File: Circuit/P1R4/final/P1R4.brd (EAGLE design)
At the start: 59.7 x 59.7 mm, 88 parts, among them J1 MICRO_USB_B_HIROSE_ZX62R-B-5P, U1 MK20DX256VLH7, U2 TPS61200, U3 MPU-9250, Y1 32.768KHz, Y2 16Mhz/8pF, Y3 26 Mhz, Y4 16 Mhz

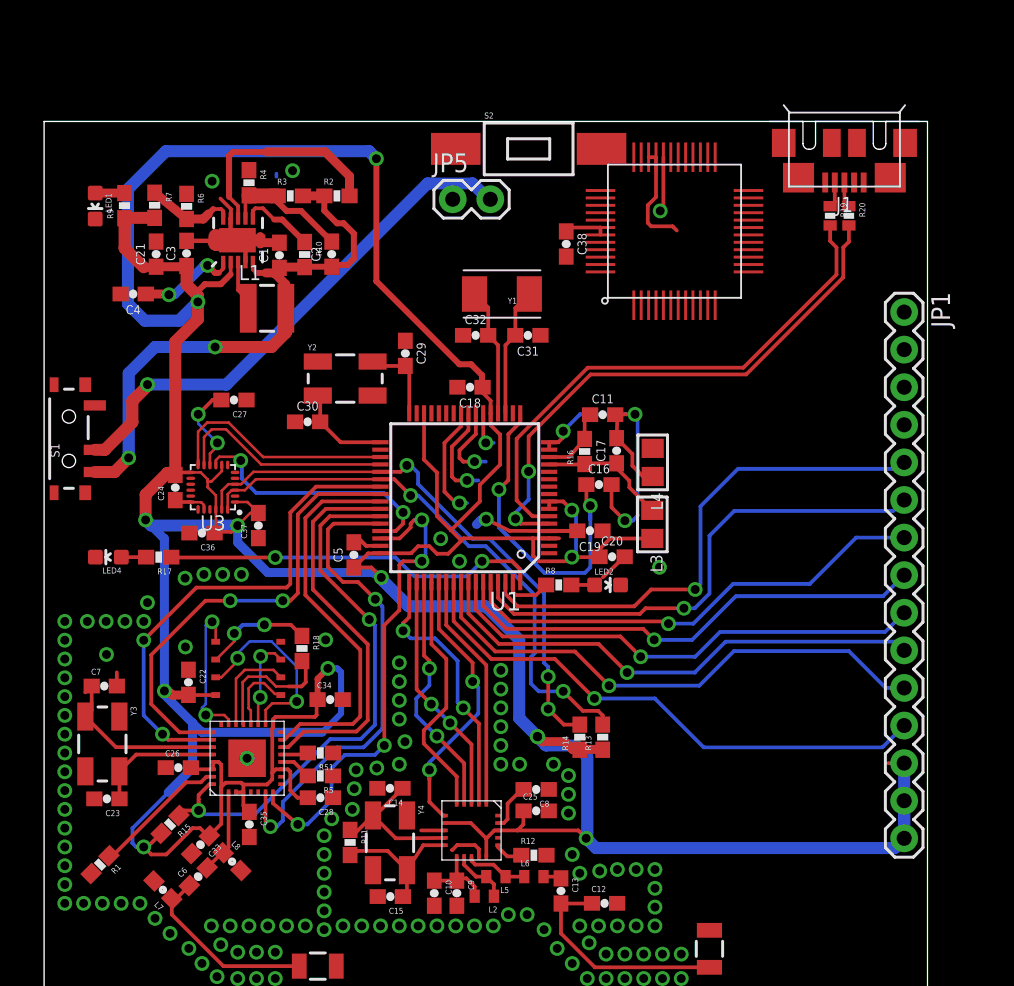
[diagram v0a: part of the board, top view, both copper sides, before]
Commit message: Added four from LED drivers to R4. Corrected R3 bootloader circuit. Rerouted switch in schematic and board on both R3 and R4 for proper isolation of USB and lipo voltage. Ready for final review
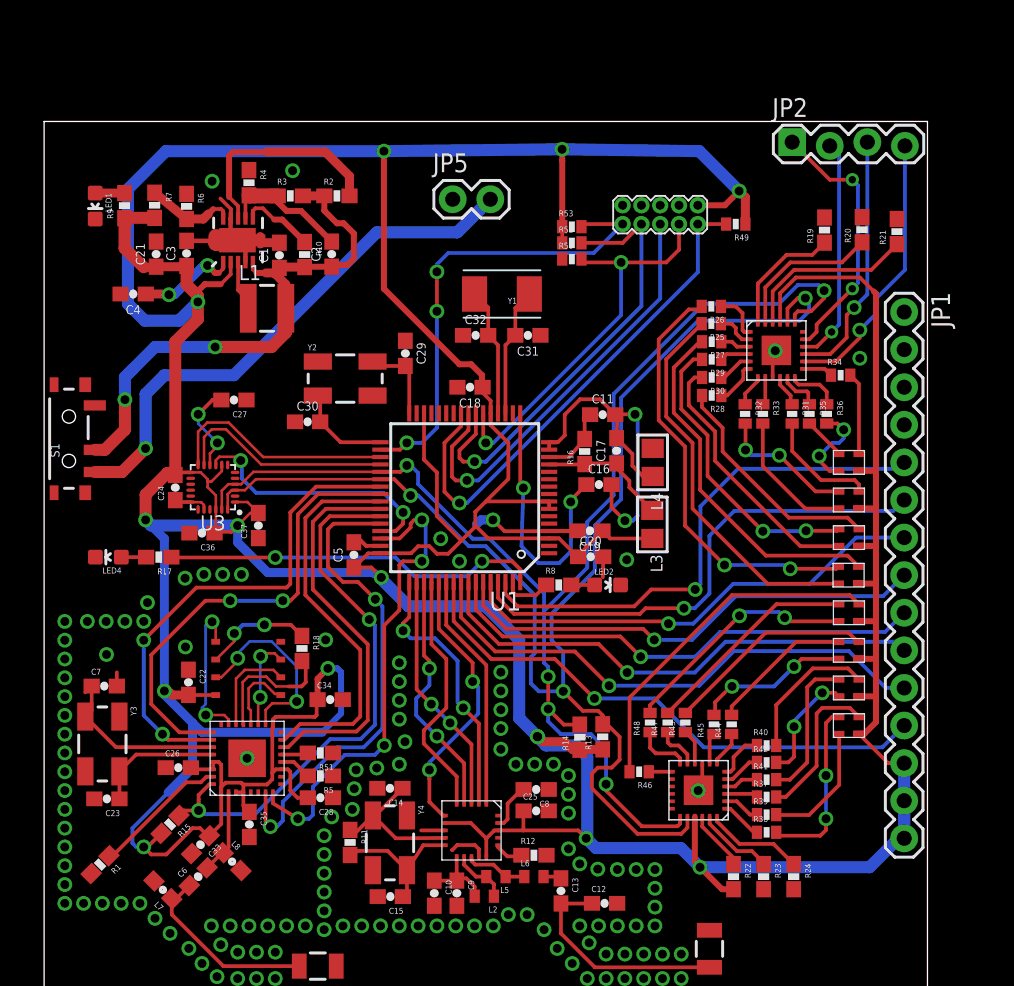
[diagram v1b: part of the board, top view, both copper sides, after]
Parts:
- removed C38: 0.1uF, appfruits:0603-CAP
- removed J1: MICRO_USB_B_HIROSE_ZX62R-B-5P, connector:USB_MICRO_B-HIROSE-ZX62R-B-5P
- removed S2: (no value), eswitch-tact:TL3302_GULL_WING
- removed U$22: MINI54TAN, TeensyCustom:MINI54TAN
- added JP2: (no value), SparkFun-Connectors:1X04_LOCK
- added R21, R22, R23, R24: 10k, SparkFun:0603-RES
- added R25, R26, R27, R28, R29, R30, R31, R32, R33, R34, R35, R36, R37, R38, R39, R40, R41, R42, R43, R44, R45, R46, R47, R48, R49, R50, R52, R53: (no value), SparkFun:0402-RES
- added U$11, U$13, U$14, U$15, U$16, U$17, U$18, U$8: LTST-C19FD1WT, led:LTST-C19FD1WT
- added U$20, U$21: PCA9552BS, NXP_By_element14_Batch_1:HVQFN24
- added U$7: 2X5_0.05"_CORTEX_DEBUGTH_NOKEY_UNSHROUDED, con-cortex:2X5_0.05"_TH_NS
- R19, R20: value 33 -> 10k; device SparkFun:0402-RES -> SparkFun:0603-RES
- moved C20 1.45 mm to (36.9, 30.3)
- moved R20 1.29 mm to (55.3, 52.4), turned to 90 degrees
- moved R19 1.04 mm to (52.7, 52.3), turned to 90 degrees
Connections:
- removed net ID: J1.4, U$22.38
- new net N$100: R39.2, U$15.G
- new net N$101: R43.1, U$21.10
- new net N$102: R47.1, U$21.11
- new net N$103: R48.1, U$21.12
- new net N$104: R46.1, U$21.13
- new net N$105: JP2.1, U$20.17
- new net N$106: R24.1, U$21.24
- new net N$107: R23.1, U$21.23
- new net N$108: R22.1, U$21.22
- new net N$109: R40.2, U$16.B
- new net N$112: R41.2, U$16.R
- new net N$113: R42.2, U$16.G
- new net N$114: R43.2, U$17.B
- new net N$115: R44.2, U$17.R
- new net N$116: R45.2, U$17.G
- new net N$117: R46.2, U$18.B
- new net N$118: R47.2, U$18.R
- new net N$119: R48.2, U$18.G
- new net N$39: R26.2, U$8.R
- new net N$40: R19.1, U$20.24
- new net N$41: R27.2, U$8.B
- new net N$42: R25.2, U$8.G
- new net N$45: R28.2, U$11.B
- new net N$46: R29.2, U$11.R
- new net N$47: R30.2, U$11.G
- new net N$48: R27.1, U$20.3
- new net N$60: R32.2, U$13.R
- new net N$61: R33.2, U$13.G
- new net N$62: R34.2, U$14.B
- new net N$63: R35.2, U$14.R
- new net N$73: R25.1, U$20.2
- new net N$76: R30.1, U$20.5
- new net N$78: R32.1, U$20.7
- new net N$79: R33.1, U$20.8
- new net N$80: R31.1, U$20.10
- new net N$81: R36.2, U$14.G
- new net N$82: R35.1, U$20.11
- new net N$83: R36.1, U$20.12
- new net N$84: R34.1, U$20.13
- new net N$85: JP2.4, U$20.14
- new net N$86: R37.2, U$15.B
- new net N$87: R20.1, U$20.23
- new net N$88: R21.1, U$20.22
- new net N$89: R38.2, U$15.R
- new net N$90: U$21.17
- new net N$91: JP2.2, U$20.16
- new net N$92: R38.1, U$21.1
- new net N$93: R39.1, U$21.2
- new net N$94: R37.1, U$21.3
- new net N$95: R41.1, U$21.4
- new net N$96: R42.1, U$21.5
- new net N$97: R40.1, U$21.6
- new net N$98: R44.1, U$21.7
- new net N$99: R45.1, U$21.8
- net 3.3V: now also R22.2, R49.1, R52.1, R53.1, U$11.V, U$13.V, U$14.V, U$15.V, U$16.V, U$17.V, U$18.V, U$20.21, U$21.21, U$7.1, U$8.V; no longer C38.1, U$22.42, U$22.43
- net GND: now also R19.2, R20.2, R21.2, R23.2, R24.2, R50.1, U$20.9, U$21.9, U$7.3, U$7.5, U$7.9; no longer C38.2, J1.5, S2.1, U$22.17, U$22.25, U$22.47, U$22.5
- net N$49: now also R26.1, U$20.1; no longer U$22.18
- net N$50: now also R31.2, U$13.B; no longer U$22.9
- net N$51: now also R28.1, U$20.6; no longer U$22.10
- net N$75: now also R29.1, U$20.4; no longer S2.2, U$22.20
- net N$8: now also JP2.3, U$20.15; no longer J1.3, R20.1
- net N$9: now also U$21.16; no longer J1.2, R19.1
- net PTA0: now also R50.2, U$7.4; no longer U$22.32
- net PTA1: now also R52.2, U$7.8
- net PTA2: now also U$7.6; no longer U$22.37
- net PTA3: now also R49.2, U$7.2; no longer U$22.33, U$22.34
- net RESET_B: now also R53.2, U$7.10; no longer U$22.8
- net SCL: now also U$20.19, U$21.19
- net SDA: now also U$20.20, U$21.20
- net USB_D_N: no longer R19.2
- net USB_D_P: no longer R20.2
- net VCC: now also S1.2; no longer J1.1, S1.1
- net VRAW: now also S1.1; no longer S1.2
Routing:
- net 3.3V: track 330.0 -> 419.2 mm, vias 13 -> 14
- net SDA: track 38.5 -> 93.9 mm, vias 2 -> 3
- net SCL: track 38.6 -> 91.0 mm, vias 3 -> 5
- net USB_D_P: track 37.7 -> 0.00 mm, vias 2 -> 0
- net USB_D_N: track 36.5 -> 0.00 mm
- net RESET_B: track 0.00 -> 32.0 mm, vias 0 -> 3
- net N$39: track 0.00 -> 28.8 mm, vias 0 -> 2
- net N$42: track 0.00 -> 26.2 mm
- net PTA1: track 5.35 -> 30.3 mm
- net N$41: track 0.00 -> 24.5 mm
- net N$117: track 0.00 -> 23.6 mm
- net PTA2: track 6.62 -> 29.0 mm
- net PTA0: track 6.31 -> 27.1 mm
- net N$46: track 0.00 -> 20.2 mm, vias 0 -> 2
- net PTA3: track 14.9 -> 34.8 mm
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
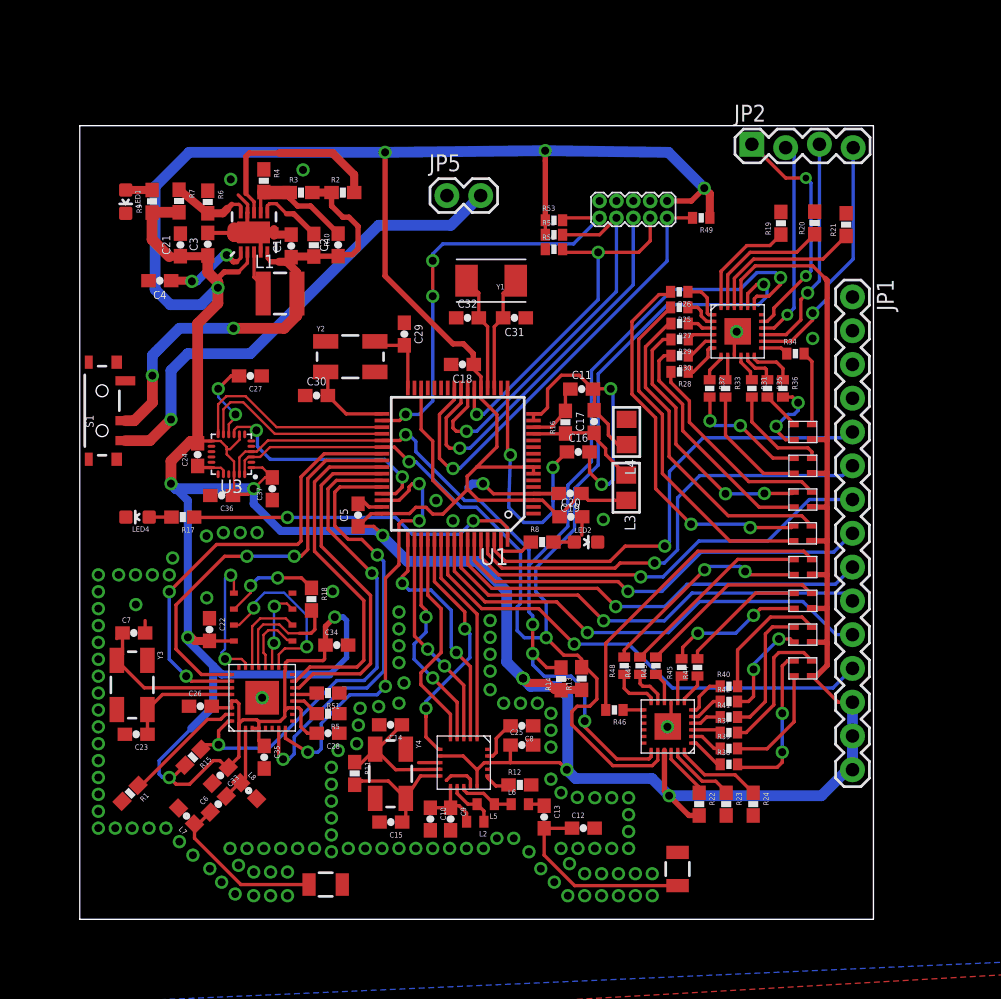
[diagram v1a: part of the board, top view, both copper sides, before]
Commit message: R3 and R4 DRC checked and ready for final review
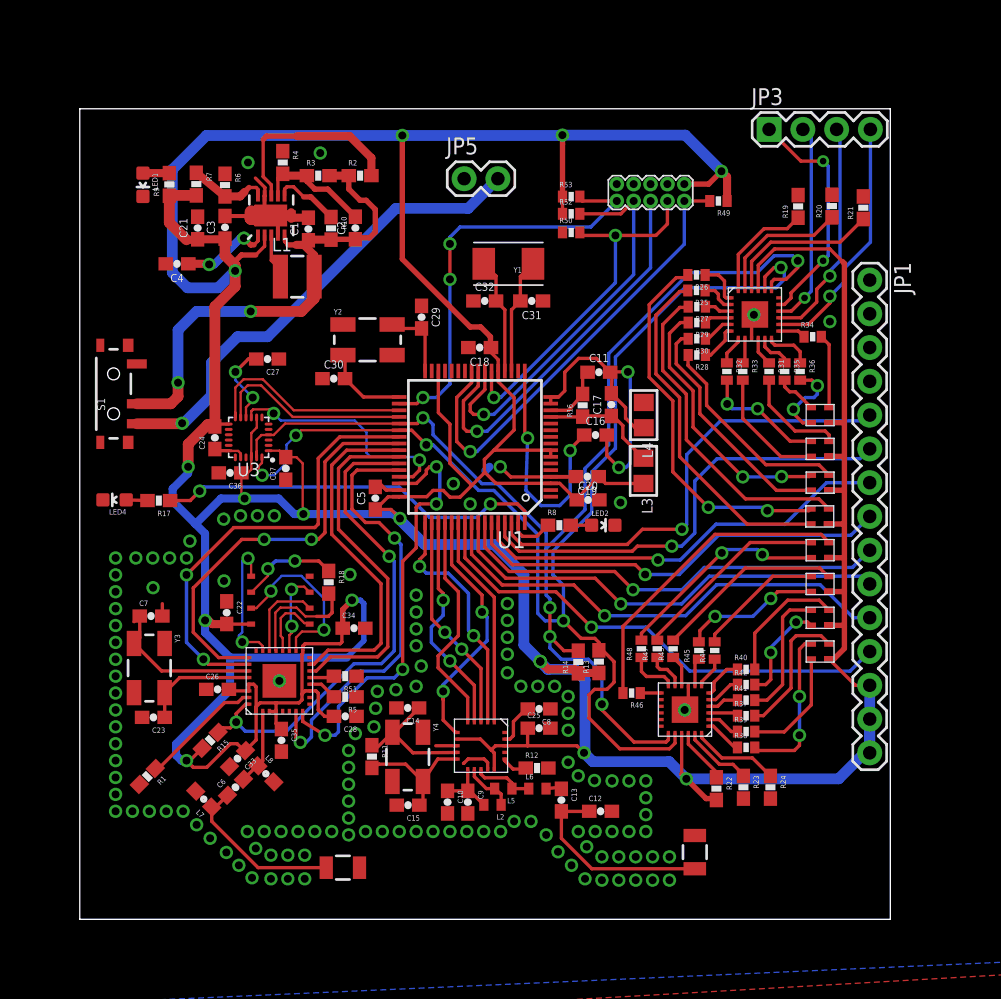
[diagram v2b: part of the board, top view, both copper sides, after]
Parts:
- removed JP2: (no value), SparkFun-Connectors:1X04_LOCK
- added JP3: (no value), SparkFun:1X04
- moved R53 2.20 mm to (37.0, 54.4)
- moved R17 2.19 mm to (5.94, 31.5)
- moved LED4 2.16 mm to (2.62, 31.5)
- moved R52 2.04 mm to (37.0, 53.1)
- moved R4 1.98 mm to (15.3, 56.9)
- moved C37 1.83 mm to (15.5, 33.9)
- moved C36 1.82 mm to (11.3, 33.6)
- moved C11 1.81 mm to (39.0, 41.1)
- moved C16 1.81 mm to (38.8, 36.4)
- moved C17 1.81 mm to (40.0, 38.7)
- moved C18 1.81 mm to (30.1, 43.0)
- moved C2 1.81 mm to (20.7, 52.0)
- moved C3 1.81 mm to (10.9, 52.0)
- moved JP1 1.81 mm to (59.4, 48.1)
- moved L3 1.81 mm to (42.4, 33.7)
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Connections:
- net N$105: now also JP3.1; no longer JP2.1
- net N$8: now also JP3.3; no longer JP2.3
- net N$85: now also JP3.4; no longer JP2.4
- net N$91: now also JP3.2; no longer JP2.2
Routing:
- net PTD7: track 25.6 -> 29.5 mm
- net SDA: track 93.9 -> 96.2 mm, vias 3 -> 5
- net GND: track 39.9 -> 37.7 mm
- net 3.3V: track 419.2 -> 421.0 mm, vias 14 -> 15
- net VCC: track 37.2 -> 38.5 mm
- net AD0: track 17.8 -> 18.5 mm
- net UVLO: track 8.79 -> 9.35 mm
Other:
- board size 59.7 x 59.7 mm -> 61 x 61 mm

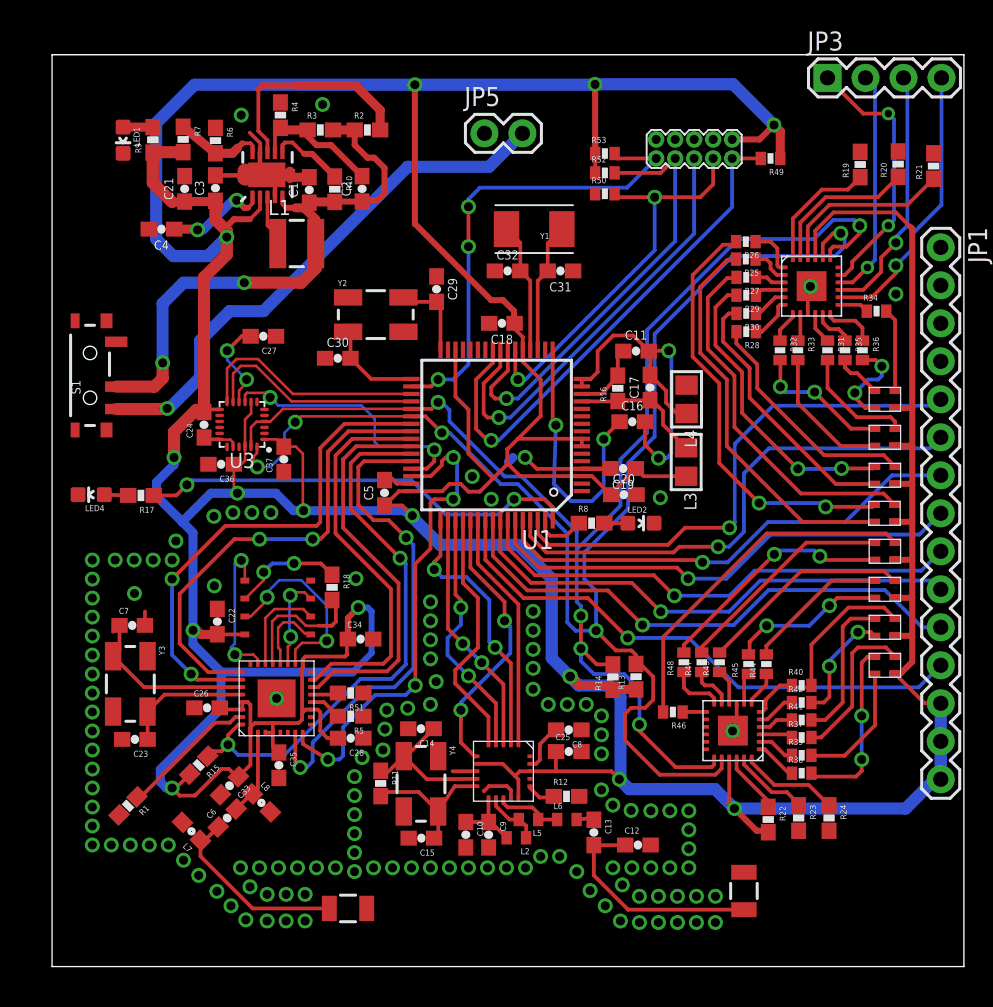
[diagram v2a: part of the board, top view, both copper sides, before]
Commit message: R3 and R4 shippable. Ordering PCBs
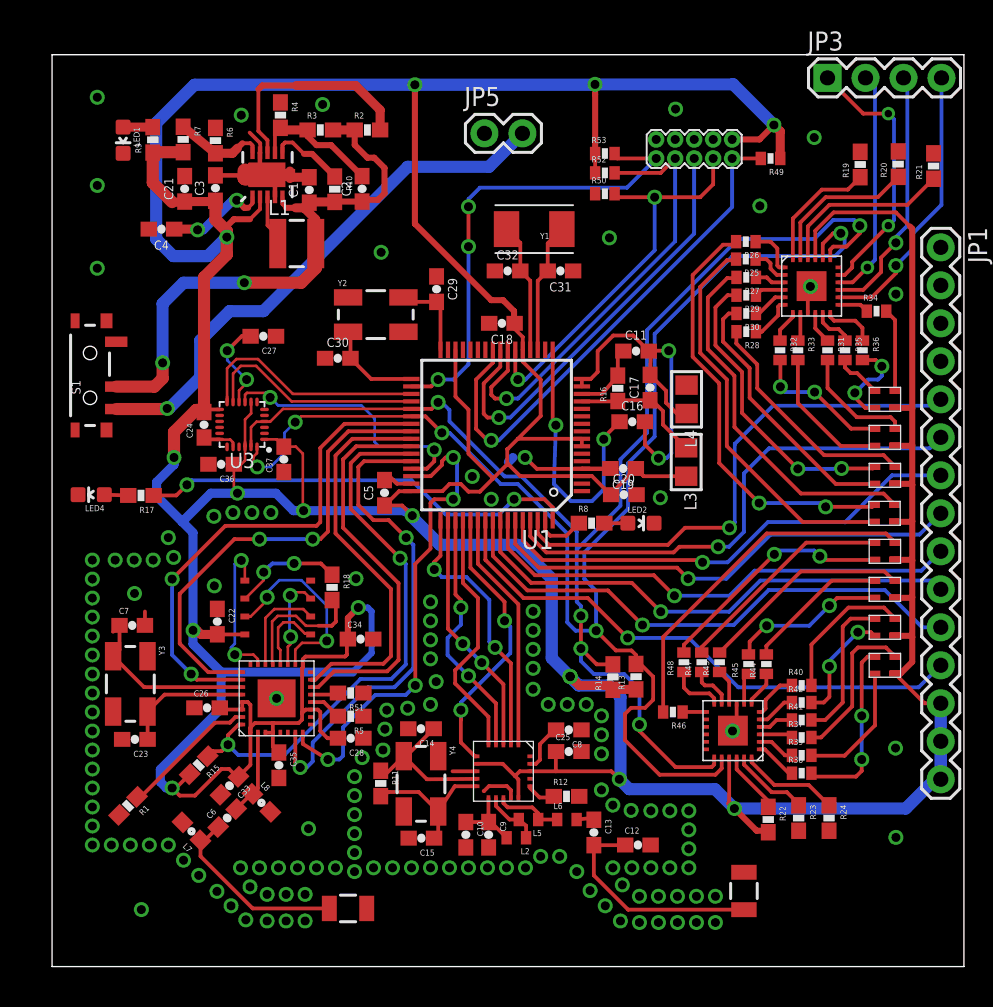
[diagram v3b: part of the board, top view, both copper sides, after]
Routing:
- net GND: vias 126 -> 139
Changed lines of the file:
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@@
 <via x="12.0904" y="30.353" extent="1-16" drill="0.6"/>
 <via x="10.8204" y="30.099" extent="1-16" drill="0.6"/>
-<via x="8.0264" y="27.178" extent="1-16" drill="0.6"/>
+<via x="8.128" y="27.3558" extent="1-16" drill="0.6"/>
 <via x="6.7564" y="27.178" extent="1-16" drill="0.6"/>
 <via x="5.4864" y="27.178" extent="1-16" drill="0.6"/>
@@
 <via x="36.9824" y="4.064" extent="1-16" drill="0.6"/>
 <via x="37.9984" y="3.048" extent="1-16" drill="0.6"/>
+<via x="56.388" y="14.605" extent="1-16" drill="0.6"/>
+<via x="56.4134" y="8.636" extent="1-16" drill="0.6"/>
+<via x="17.145" y="9.2202" extent="1-16" drill="0.6"/>
+<via x="5.969" y="3.81" extent="1-16" drill="0.6"/>
+<via x="7.7724" y="28.6766" extent="1-16" drill="0.6"/>
+<via x="3.0226" y="46.6852" extent="1-16" drill="0.6"/>
+<via x="3.0226" y="52.2224" extent="1-16" drill="0.6"/>
+<via x="3.0226" y="58.1152" extent="1-16" drill="0.6"/>
+<via x="21.9964" y="47.752" extent="1-16" drill="0.6"/>
+<via x="37.2618" y="48.7172" extent="1-16" drill="0.6"/>
+<via x="41.6814" y="57.3278" extent="1-16" drill="0.6"/>
+<via x="50.9524" y="55.4228" extent="1-16" drill="0.6"/>
+<via x="47.3202" y="50.8508" extent="1-16" drill="0.6"/>
 </signal>
 <signal name="N$2">
@@
 <wire x1="19.4564" y1="16.002" x2="21.6154" y2="18.161" width="0.254" layer="16"/>
 </signal>
-<signal name="N$110">
-<via x="8.2804" y="28.448" extent="1-16" drill="0.6"/>
-</signal>
 <signal name="N$132">

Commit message: Added some part names to P1R4 to make assembly suck less
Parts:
- moved Y1 1.90 mm to (33.1, 47.6)
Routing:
- net N$10: track 8.74 -> 9.37 mm
- net N$11: track 8.72 -> 8.17 mm

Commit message: Gerbers generated
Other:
- board text added: "U2"
- board text added: "U4"
- board text added: "U6"
- board text added: "u20"
- board text added: "u21"
